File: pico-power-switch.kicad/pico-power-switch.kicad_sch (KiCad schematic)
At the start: 18 parts, among them J1 JST-PH2 Bat, J2 Pico Pin 1-13, J3 Pico Pin 40-28, J4 Alt-Bat, J5 Stemma-QT_Qwicc, Q1 AO3401A, Q2 AO3401A, SW1 SW_Push_SLIM, U1 74LVC2G74, U2 PCF8563T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

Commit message: Rev 1.0 (in production)
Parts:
- J5: now left out of the parts list
- Q1, Q2: LCSC (none) -> C15127
- U1: LCSC C6762 -> C282355
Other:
- note added: "Stemma/Qt"
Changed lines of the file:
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@@
   (title_block
     (title "pico-power-switch")
-    (date "2023-05-25")
+    (date "2023-06-10")
     (rev "1.0")
     (company "Bernhard Bablok")
@@
   )
   (junction (at 216.916 57.15) (diameter 0) (color 0 0 0 0)
-  )
-  (junction (at 168.91 106.68) (diameter 0) (color 0 0 0 0)
   )
   (no_connect (at 88.9 128.27))
@@
     (stroke (width 0) (type default) (color 0 0 0 0))
   )
+  (polyline (pts (xy 141.732 164.084) (xy 73.152 164.084))
+    (stroke (width 0) (type default) (color 0 0 0 0))
+  )
   (wire (pts (xy 85.09 138.43) (xy 88.9 138.43))
     (stroke (width 0) (type default) (color 0 0 0 0))
@@
     (stroke (width 0) (type default) (color 0 0 0 0))
   )
+  (polyline (pts (xy 141.732 144.526) (xy 141.732 164.084))
+    (stroke (width 0) (type default) (color 0 0 0 0))
+  )
   (wire (pts (xy 82.55 107.95) (xy 88.9 107.95))
     (stroke (width 0) (type default) (color 0 0 0 0))
@@
     (stroke (width 0) (type default) (color 0 0 0 0))
   )
+  (wire (pts (xy 168.91 106.68) (xy 168.91 113.03))
+    (stroke (width 0) (type default) (color 0 0 0 0))
+  )
   (wire (pts (xy 93.98 55.88) (xy 98.552 55.88))
     (stroke (width 0) (type default) (color 0 0 0 0))
@@
     (stroke (width 0) (type default) (color 0 0 0 0))
   )
+  (polyline (pts (xy 73.152 144.526) (xy 73.152 164.084))
+    (stroke (width 0) (type default) (color 0 0 0 0))
+  )
   (wire (pts (xy 98.552 55.88) (xy 98.552 58.42))
     (stroke (width 0) (type default) (color 0 0 0 0))
@@
     (stroke (width 0) (type default) (color 0 0 0 0))
   )
-  (wire (pts (xy 168.91 106.68) (xy 168.91 113.03))
-    (stroke (width 0) (type default) (color 0 0 0 0))
-  )
   (wire (pts (xy 180.34 59.182) (xy 180.34 62.23))
     (stroke (width 0) (type default) (color 0 0 0 0))
   )
   (wire (pts (xy 188.722 46.99) (xy 192.786 46.99))
+    (stroke (width 0) (type default) (color 0 0 0 0))
+  )
+  (polyline (pts (xy 73.152 144.526) (xy 141.732 144.526))
     (stroke (width 0) (type default) (color 0 0 0 0))
   )
@@
   )
   (text "RTC: on: high->low" (at 75.565 93.345 0)
+    (effects (font (size 1.27 1.27)) (justify left bottom))
+  )
+  (text "Stemma/Qt" (at 74.168 163.322 0)
     (effects (font (size 1.27 1.27)) (justify left bottom))
   )
@@
   )
   (symbol (lib_id "user:Stemma-QT_Qwicc") (at 106.426 155.194 0) (unit 1)
-    (in_bom yes) (on_board yes)
+    (in_bom no) (on_board yes)
     (property "Reference" "J5" (id 0) (at 107.442 146.558 0)
       (effects (font (size 1.27 1.27)) (justify left))
@@
     (property "Datasheet" "http://www.aosmd.com/pdfs/datasheet/AO3401A.pdf" (id 3) (at 207.01 132.334 0)
       (effects (font (size 1.27 1.27)) (justify left) hide)
+    )
+    (property "LCSC" "C15127 " (id 4) (at 207.01 132.334 0)
+      (effects (font (size 1.27 1.27)) hide)
     )
     (pin "1")
@@
       (effects (font (size 1.524 1.524)) (justify left) hide)
     )
-    (property "LCSC" "C6762" (id 13) (at 203.2 66.04 0)
+    (property "LCSC" "C282355 " (id 13) (at 203.2 66.04 0)
       (effects (font (size 1.27 1.27)) hide)
     )
@@
       (effects (font (size 1.27 1.27)) (justify left) hide)
     )
-    (pin "1")
+    (property "LCSC" "C15127 " (id 4) (at 183.134 132.334 0)
+      (effects (font (size 1.27 1.27)) hide)
+    )
+    (pin "1")

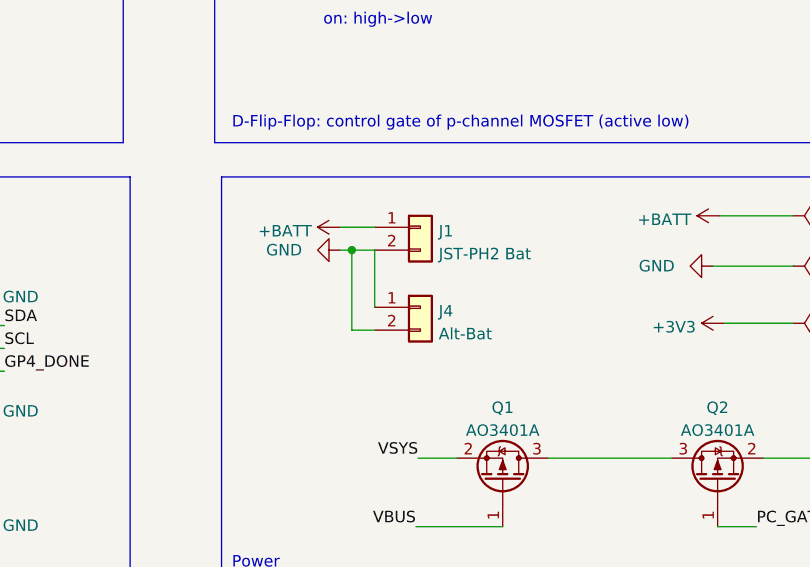
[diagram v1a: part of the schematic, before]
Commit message: fixed schematic for power-connectors
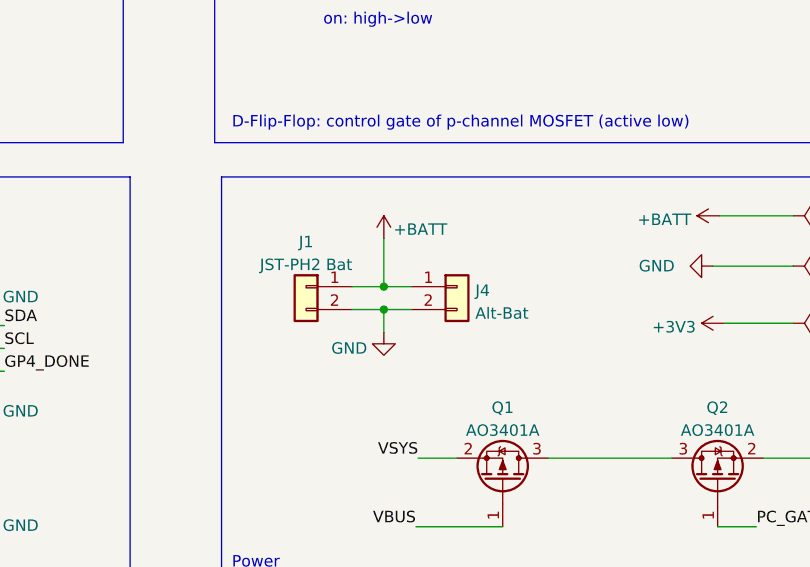
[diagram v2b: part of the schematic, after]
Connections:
- net +BATT: now also J4.1 (Pin_1)
- net GND: no longer J4.1 (Pin_1)
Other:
- moved on the sheet: J1, J4
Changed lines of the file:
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@@
   (title_block
     (title "pico-power-switch")
-    (date "2023-06-10")
+    (date "2023-06-20")
     (rev "1.0")
     (company "Bernhard Bablok")
@@
   (junction (at 188.722 57.15) (diameter 0) (color 0 0 0 0)
   )
+  (junction (at 169.926 110.744) (diameter 0) (color 0 0 0 0)
+  )
   (junction (at 180.34 62.23) (diameter 0) (color 0 0 0 0)
   )
+  (junction (at 169.926 113.284) (diameter 0) (color 0 0 0 0)
+  )
   (junction (at 111.76 50.8) (diameter 0) (color 0 0 0 0)
   )
   (junction (at 216.916 64.77) (diameter 0) (color 0 0 0 0)
-  )
-  (junction (at 166.37 106.68) (diameter 0) (color 0 0 0 0)
   )
   (junction (at 216.916 57.15) (diameter 0) (color 0 0 0 0)
@@
     (stroke (width 0) (type default) (color 0 0 0 0))
   )
-  (wire (pts (xy 166.37 106.68) (xy 166.37 115.57))
-    (stroke (width 0) (type default) (color 0 0 0 0))
-  )
   (wire (pts (xy 216.916 64.77) (xy 218.694 64.77))
     (stroke (width 0) (type default) (color 0 0 0 0))
@@
     (stroke (width 0) (type default) (color 0 0 0 0))
   )
-  (wire (pts (xy 168.91 115.57) (xy 166.37 115.57))
+  (wire (pts (xy 166.37 113.284) (xy 169.926 113.284))
     (stroke (width 0) (type default) (color 0 0 0 0))
   )
@@
     (stroke (width 0) (type default) (color 0 0 0 0))
   )
+  (wire (pts (xy 169.926 113.284) (xy 172.974 113.284))
+    (stroke (width 0) (type default) (color 0 0 0 0))
+  )
   (polyline (pts (xy 73.152 98.552) (xy 141.732 98.552))
     (stroke (width 0) (type default) (color 0 0 0 0))
@@
     (stroke (width 0) (type default) (color 0 0 0 0))
   )
-  (wire (pts (xy 166.37 106.68) (xy 168.91 106.68))
-    (stroke (width 0) (type default) (color 0 0 0 0))
-  )
   (polyline (pts (xy 151.892 98.552) (xy 231.14 98.552))
     (stroke (width 0) (type default) (color 0 0 0 0))
   )
-  (wire (pts (xy 168.91 106.68) (xy 168.91 113.03))
-    (stroke (width 0) (type default) (color 0 0 0 0))
-  )
   (wire (pts (xy 93.98 55.88) (xy 98.552 55.88))
     (stroke (width 0) (type default) (color 0 0 0 0))
@@
     (stroke (width 0) (type default) (color 0 0 0 0))
   )
-  (wire (pts (xy 165.1 104.14) (xy 168.91 104.14))
-    (stroke (width 0) (type default) (color 0 0 0 0))
-  )
   (wire (pts (xy 85.852 55.88) (xy 88.9 55.88))
     (stroke (width 0) (type default) (color 0 0 0 0))
@@
     (stroke (width 0) (type default) (color 0 0 0 0))
   )
+  (wire (pts (xy 169.926 105.41) (xy 169.926 110.744))
+    (stroke (width 0) (type default) (color 0 0 0 0))
+  )
   (wire (pts (xy 123.952 117.602) (xy 127.762 117.602))
     (stroke (width 0) (type default) (color 0 0 0 0))
@@
     (stroke (width 0) (type default) (color 0 0 0 0))
   )
+  (wire (pts (xy 169.926 113.284) (xy 169.926 115.824))
+    (stroke (width 0) (type default) (color 0 0 0 0))
+  )
   (wire (pts (xy 208.28 64.77) (xy 216.916 64.77))
     (stroke (width 0) (type default) (color 0 0 0 0))
@@
     (stroke (width 0) (type default) (color 0 0 0 0))
   )
+  (wire (pts (xy 166.37 110.744) (xy 169.926 110.744))
+    (stroke (width 0) (type default) (color 0 0 0 0))
+  )
   (wire (pts (xy 127.762 58.42) (xy 121.92 58.42))
     (stroke (width 0) (type default) (color 0 0 0 0))
   )
+  (wire (pts (xy 169.926 110.744) (xy 172.974 110.744))
+    (stroke (width 0) (type default) (color 0 0 0 0))
+  )
   (wire (pts (xy 216.916 63.754) (xy 216.916 64.77))
     (stroke (width 0) (type default) (color 0 0 0 0))
@@
   )
   (wire (pts (xy 99.06 88.9) (xy 93.98 88.9))
-    (stroke (width 0) (type default) (color 0 0 0 0))
-  )
-  (wire (pts (xy 165.1 106.68) (xy 166.37 106.68))
     (stroke (width 0) (type default) (color 0 0 0 0))
   )
@@
     (pin "2")
   )
-  (symbol (lib_id "Connector_Generic:Conn_01x02") (at 173.99 104.14 0) (unit 1)
+  (symbol (lib_id "Connector_Generic:Conn_01x02") (at 161.29 110.744 0) (mirror y) (unit 1)
     (in_bom no) (on_board yes) (fields_autoplaced)
-    (property "Reference" "J1" (id 0) (at 176.022 104.5753 0)
-      (effects (font (size 1.27 1.27)) (justify left))
-    )
-    (property "Value" "JST-PH2 Bat" (id 1) (at 176.022 107.1122 0)
-      (effects (font (size 1.27 1.27)) (justify left))
-    )
-    (property "Footprint" "Connector_JST:JST_PH_S2B-PH-SM4-TB_1x02-1MP_P2.00mm_Horizontal" (id 2) (at 173.99 104.14 0)
-      (effects (font (size 1.27 1.27)) hide)
-    )
-    (property "Datasheet" "~" (id 3) (at 173.99 104.14 0)
+    (property "Reference" "J1" (id 0) (at 161.29 105.7742 0))
+    (property "Value" "JST-PH2 Bat" (id 1) (at 161.29 108.3111 0))
+    (property "Footprint" "Connector_JST:JST_PH_S2B-PH-SM4-TB_1x02-1MP_P2.00mm_Horizontal" (id 2) (at 161.29 110.744 0)
+      (effects (font (size 1.27 1.27)) hide)
+    )
+    (property "Datasheet" "~" (id 3) (at 161.29 110.744 0)
       (effects (font (size 1.27 1.27)) hide)
     )
@@
     (pin "2")
   )
-  (symbol (lib_id "power:GND") (at 165.1 106.68 270) (unit 1)
-    (in_bom yes) (on_board yes)
-    (property "Reference" "#PWR013" (id 0) (at 158.75 106.68 0)
-      (effects (font (size 1.27 1.27)) hide)
-    )
-    (property "Value" "GND" (id 1) (at 156.845 106.68 90)
-      (effects (font (size 1.27 1.27)) (justify left))
-    )
-    (property "Footprint" "" (id 2) (at 165.1 106.68 0)
-      (effects (font (size 1.27 1.27)) hide)
-    )
-    (property "Datasheet" "" (id 3) (at 165.1 106.68 0)
+  (symbol (lib_id "power:GND") (at 169.926 115.824 0) (unit 1)
+    (in_bom yes) (on_board yes)
+    (property "Reference" "#PWR013" (id 0) (at 169.926 122.174 0)
+      (effects (font (size 1.27 1.27)) hide)
+    )
+    (property "Value" "GND" (id 1) (at 164.084 117.602 0)
+      (effects (font (size 1.27 1.27)) (justify left))
+    )
+    (property "Footprint" "" (id 2) (at 169.926 115.824 0)
+      (effects (font (size 1.27 1.27)) hide)
+    )
+    (property "Datasheet" "" (id 3) (at 169.926 115.824 0)
       (effects (font (size 1.27 1.27)) hide)
     )
@@
     (pin "1")
   )
-  (symbol (lib_id "Connector_Generic:Conn_01x02") (at 173.99 113.03 0) (unit 1)
+  (symbol (lib_id "Connector_Generic:Conn_01x02") (at 178.054 110.744 0) (unit 1)
     (in_bom no) (on_board yes) (fields_autoplaced)
-    (property "Reference" "J4" (id 0) (at 176.022 113.4653 0)
-      (effects (font (size 1.27 1.27)) (justify left))
-    )
-    (property "Value" "Alt-Bat" (id 1) (at 176.022 116.0022 0)
-      (effects (font (size 1.27 1.27)) (justify left))
-    )
-    (property "Footprint" "Connector_PinHeader_2.54mm:PinHeader_1x02_P2.54mm_Vertical" (id 2) (at 173.99 113.03 0)
-      (effects (font (size 1.27 1.27)) hide)
-    )
-    (property "Datasheet" "~" (id 3) (at 173.99 113.03 0)
+    (property "Reference" "J4" (id 0) (at 180.086 111.1793 0)
+      (effects (font (size 1.27 1.27)) (justify left))
+    )
+    (property "Value" "Alt-Bat" (id 1) (at 180.086 113.7162 0)
+      (effects (font (size 1.27 1.27)) (justify left))
+    )
+    (property "Footprint" "Connector_PinHeader_2.54mm:PinHeader_1x02_P2.54mm_Vertical" (id 2) (at 178.054 110.744 0)
+      (effects (font (size 1.27 1.27)) hide)
+    )
+    (property "Datasheet" "~" (id 3) (at 178.054 110.744 0)
       (effects (font (size 1.27 1.27)) hide)
     )
@@
     (pin "1")
   )
-  (symbol (lib_id "power:+BATT") (at 165.1 104.14 90) (unit 1)
-    (in_bom yes) (on_board yes) (fields_autoplaced)
-    (property "Reference" "#PWR012" (id 0) (at 168.91 104.14 0)
-      (effects (font (size 1.27 1.27)) hide)
-    )
-    (property "Value" "+BATT" (id 1) (at 161.925 104.5738 90)
-      (effects (font (size 1.27 1.27)) (justify left))
-    )
-    (property "Footprint" "" (id 2) (at 165.1 104.14 0)
-      (effects (font (size 1.27 1.27)) hide)
-    )
-    (property "Datasheet" "" (id 3) (at 165.1 104.14 0)
-      (effects (font (size 1.27 1.27)) hide)
-    )
+  (symbol (lib_id "power:+BATT") (at 169.926 105.41 0) (unit 1)
+    (in_bom yes) (on_board yes)
+    (property "Reference" "#PWR012" (id 0) (at 169.926 109.22 0)
+      (effects (font (size 1.27 1.27)) hide)
+    )
+    (property "Value" "+BATT" (id 1) (at 173.99 104.394 0))
+    (property "Footprint" "" (id 2) (at 169.926 105.41 0)
+      (effects (font (size 1.27 1.27)) hide)
+    )
+    (property "Datasheet" "" (id 3) (at 169.926 105.41 0)
+      (effects (font (size 1.27 1.27)) hide)
+    )
